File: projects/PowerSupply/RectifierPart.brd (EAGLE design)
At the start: 80 x 45 mm, 12 parts, among them X1 IN, X2 PRI, X3 SEC, X4 OUT

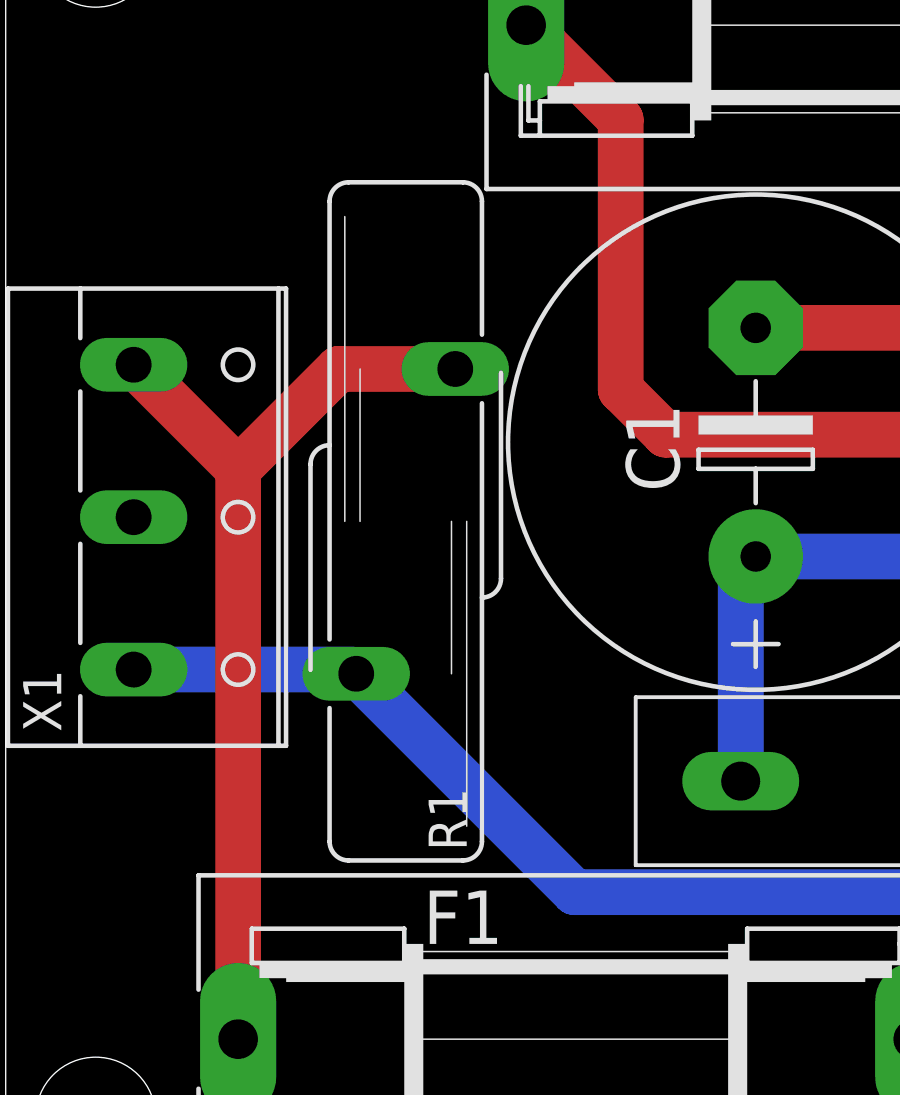
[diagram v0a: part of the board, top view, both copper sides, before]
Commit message: fix(rect): replaced s20k275 with s20k230
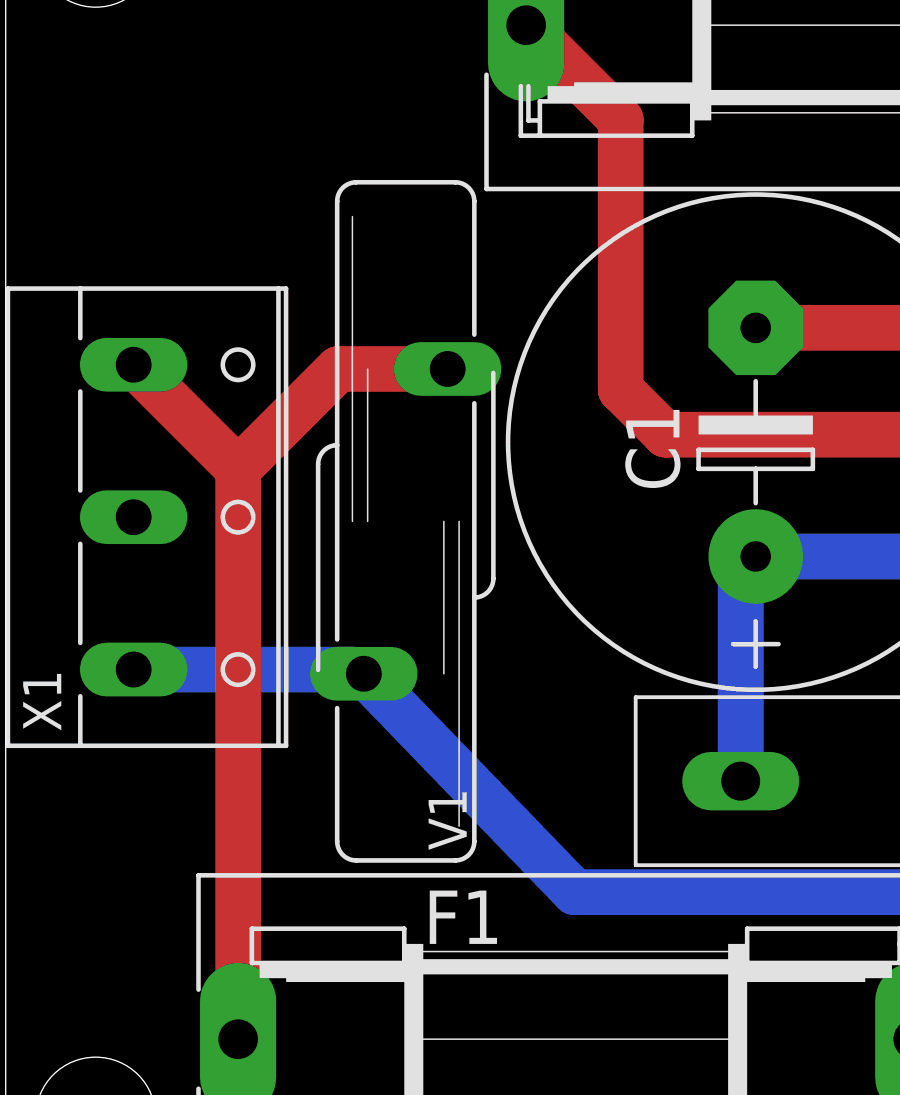
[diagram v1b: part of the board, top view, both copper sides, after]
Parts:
- removed R1: S20K275, varistor:S20K275
- added V1: S20K230, varistor:S20K230
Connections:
- net +230VAC: now also V1.2; no longer R1.2
- net -230VAC: now also V1.1; no longer R1.1
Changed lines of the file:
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@@
 <attribute name="VALUE" x="28.5746" y="42.575" size="1.778" layer="27" ratio="10"/>
 </element>
-<element name="R1" library="varistor" library_urn="urn:adsk.eagle:library:410" package="S20K275" package3d_urn="urn:adsk.eagle:package:30604/1" value="S20K275" x="13.335" y="22.86" smashed="yes">
+<element name="V1" library="varistor" library_urn="urn:adsk.eagle:library:410" package="S20K230" package3d_urn="urn:adsk.eagle:package:30579/1" value="S20K230" x="13.335" y="22.86" smashed="yes">
 <attribute name="NAME" x="14.097" y="13.97" size="1.27" layer="25" ratio="10" rot="R270"/>
 <attribute name="POPULARITY" value="0" x="29.845" y="11.43" size="1.778" layer="27" display="off"/>
@@
 <contactref element="X1" pad="1"/>
 <contactref element="F1" pad="2"/>
-<contactref element="R1" pad="2"/>
+<contactref element="V1" pad="2"/>
 <wire x1="7.7478" y1="5.6" x2="7.7478" y2="24.5972" width="1.524" layer="1"/>
 <wire x1="7.7478" y1="24.5972" x2="4.265" y2="28.08" width="1.524" layer="1"/>
-<wire x1="14.986" y1="27.94" x2="11.0906" y2="27.94" width="1.524" layer="1"/>
+<wire x1="14.732" y1="27.94" x2="11.0906" y2="27.94" width="1.524" layer="1"/>
 <wire x1="11.0906" y1="27.94" x2="7.7478" y2="24.5972" width="1.524" layer="1"/>
 </signal>
 <signal name="-230VAC">
 <contactref element="X1" pad="3"/>
-<contactref element="R1" pad="1"/>
+<contactref element="V1" pad="1"/>
 <contactref element="X2" pad="4"/>
 <wire x1="4.265" y1="17.92" x2="11.544" y2="17.92" width="1.524" layer="16"/>
-<wire x1="11.544" y1="17.92" x2="11.684" y2="17.78" width="1.524" layer="16"/>
-<wire x1="11.684" y1="17.78" x2="18.964" y2="10.5" width="1.524" layer="16"/>
+<wire x1="11.544" y1="17.92" x2="11.938" y2="17.78" width="1.524" layer="16"/>
+<wire x1="11.938" y1="17.78" x2="18.964" y2="10.5" width="1.524" layer="16"/>
 <wire x1="18.964" y1="10.5" x2="44" y2="10.5" width="1.524" layer="16"/>
 <wire x1="44" y1="10.5" x2="49.62" y2="4.88" width="1.524" layer="16"/>

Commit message: feat: rectifier fuse values modified
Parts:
- F1: value 1.5A -> 1.6AT
- F2: value 10A -> 6.3AT
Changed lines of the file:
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@@
 <attribute name="VALUE" x="60.2926" y="31.19" size="1.778" layer="27" ratio="10" rot="R90"/>
 </element>
-<element name="F1" library="fuse" library_urn="urn:adsk.eagle:library:233" package="SH22,5A" package3d_urn="urn:adsk.eagle:package:14070/1" value="1.5A" x="19" y="5.6" smashed="yes" rot="R180">
+<element name="F1" library="fuse" library_urn="urn:adsk.eagle:library:233" package="SH22,5A" package3d_urn="urn:adsk.eagle:package:14070/1" value="1.6AT" x="19" y="5.6" smashed="yes" rot="R180">
 <attribute name="MF" value="" x="-6.4" y="55.13" size="1.778" layer="27" rot="R180" display="off"/>
 <attribute name="MPN" value="0031.7701.11" x="-6.4" y="55.13" size="1.778" layer="27" rot="R180" display="off"/>
@@
 <attribute name="VALUE" x="18.3396" y="8.775" size="1.778" layer="27" ratio="10"/>
 </element>
-<element name="F2" library="fuse" library_urn="urn:adsk.eagle:library:233" package="SH22,5A" package3d_urn="urn:adsk.eagle:package:14070/1" value="10A" x="28.6" y="39.4" smashed="yes" rot="R180">
+<element name="F2" library="fuse" library_urn="urn:adsk.eagle:library:233" package="SH22,5A" package3d_urn="urn:adsk.eagle:package:14070/1" value="6.3AT" x="28.6" y="39.4" smashed="yes" rot="R180">
 <attribute name="MF" value="" x="-23.47" y="88.93" size="1.778" layer="27" rot="R180" display="off"/>
 <attribute name="MPN" value="0031.7701.11" x="-23.47" y="88.93" size="1.778" layer="27" rot="R180" display="off"/>
